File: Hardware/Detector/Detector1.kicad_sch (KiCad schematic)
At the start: 27 parts, among them J1 Conn_Coaxial, U1 OPA145ID, U2 OPA145ID, U3 OPA145ID

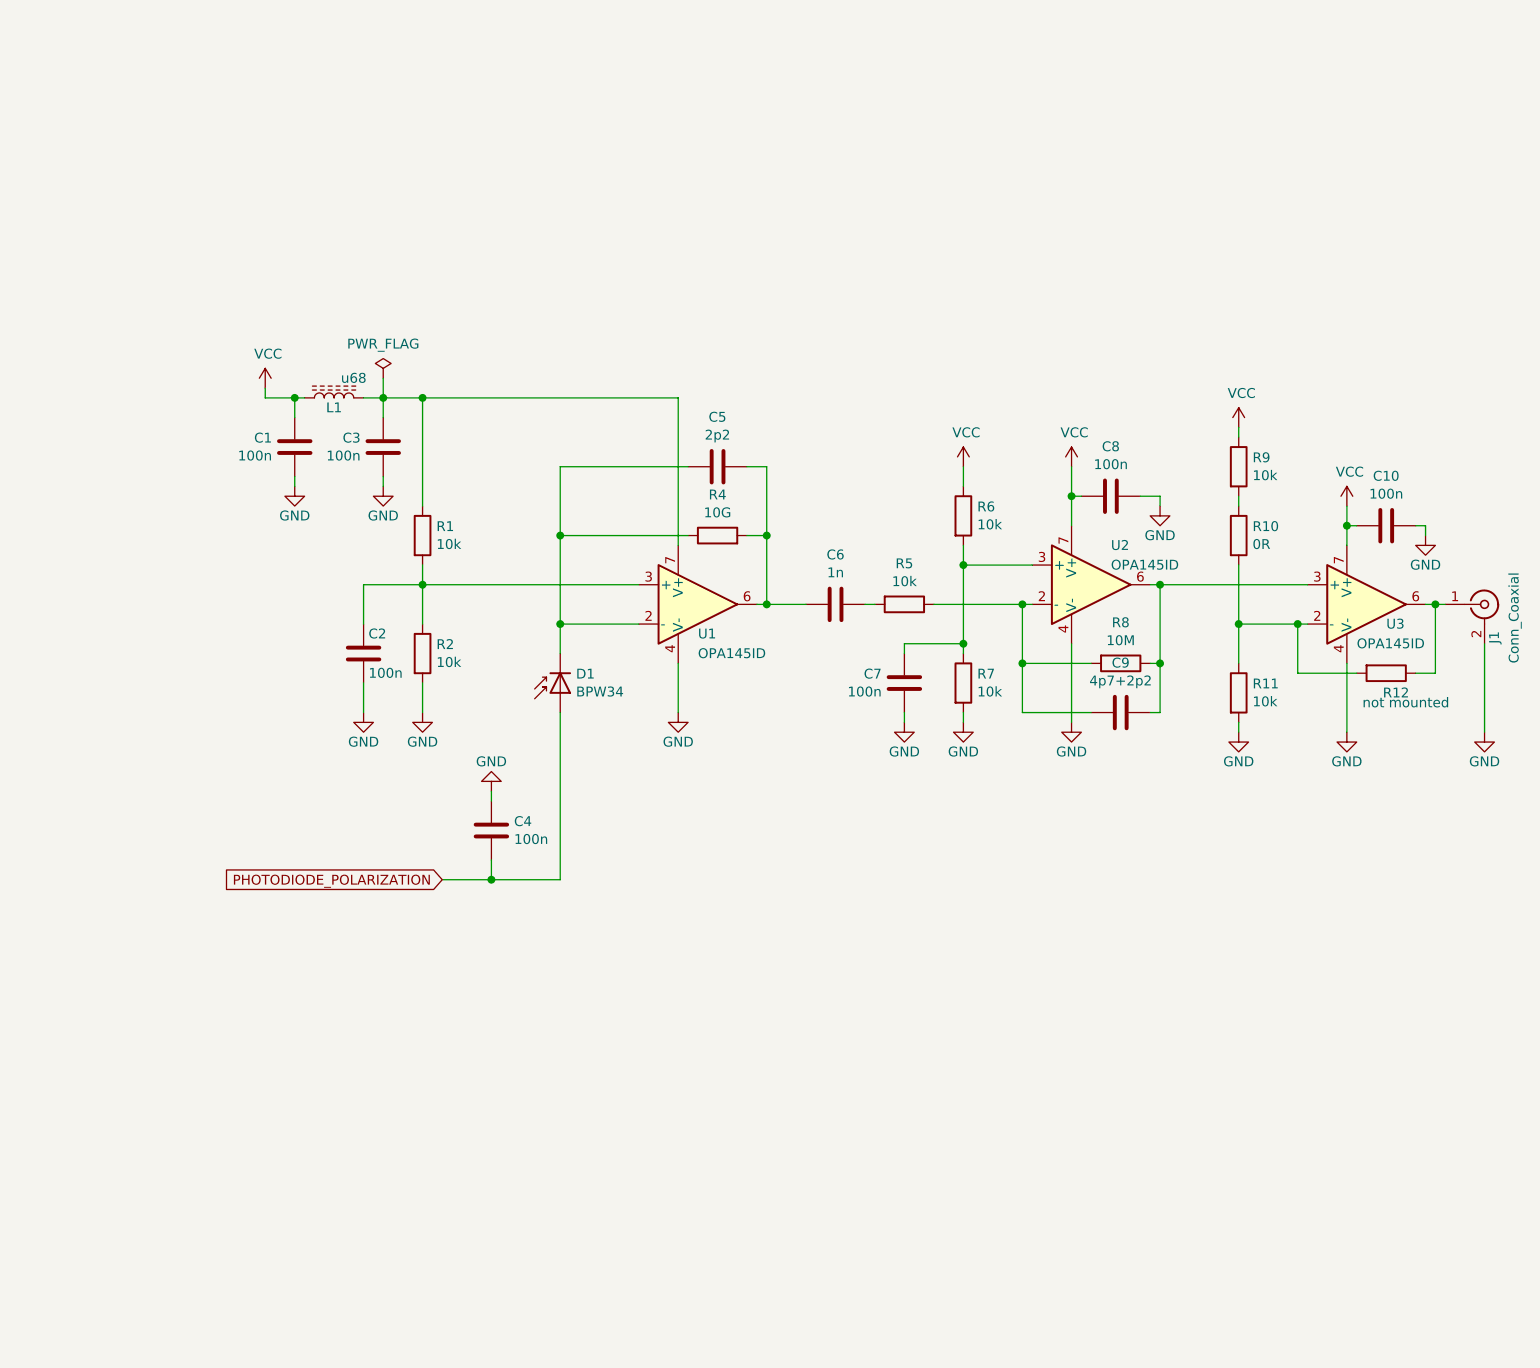
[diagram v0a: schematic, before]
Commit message: switch to low cost solution
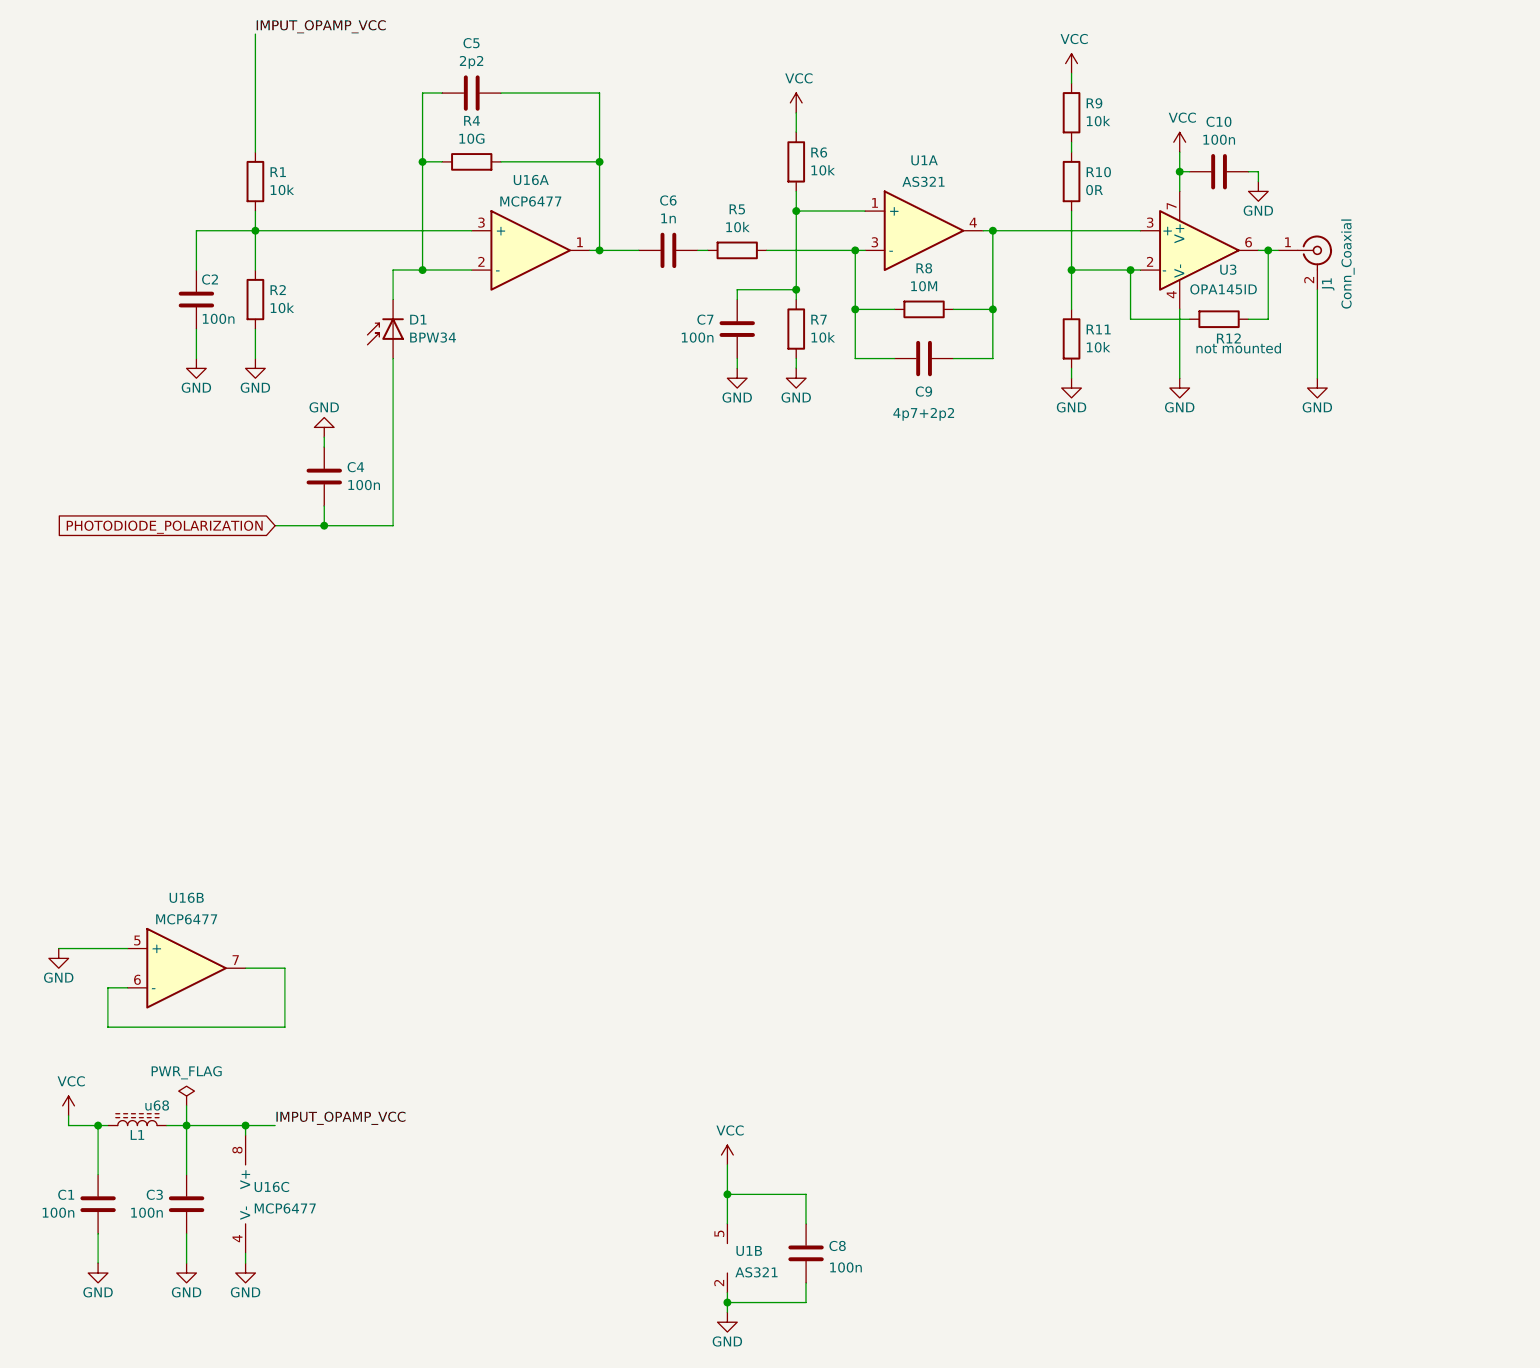
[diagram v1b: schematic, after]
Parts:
- removed U1, U2: OPA145ID, Package_SO:SOIC-8_3.9x4.9mm_P1.27mm, symbol OPA145ID:OPA145ID
- added U1: AS321, Package_TO_SOT_SMD:SOT-223-5, symbol DiscretePixelDetectorForRadiationAnalysis:AS321
- added U16: MCP6477, symbol Device:Opamp_Dual_Generic
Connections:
- net GND: now also C8.2, U1.2, U16.4 (V-), U16.5 (+); no longer C8.1
- net VCC: now also C8.1, U1.5; no longer C8.2
- net at C2.1, R1.2, R2.1: now also U16.3 (+)
- net at C5.1, C6.2, R4.2: now also U16.1
- net IMPUT_OPAMP_VCC: now reaches C3.1, L1.1, R1.1
- net IMPUT_OPAMP_VCC: now also U16.8 (V+)
- net at C7.1, R6.2, R7.1: now also U1.1 (+)
- net at C9.1, R8.1, U3.3 (+): now also U1.4
- net at C9.2, R5.1, R8.2: now also U1.3 (-)
- net at C5.2, D1.1 (K), R4.1: now also U16.2 (-)
- new net: U16.6 (-), U16.7
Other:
- moved on the sheet: C1, C10, C2, C3, C4, C5, C6, C7, C8, C9, D1, J1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
